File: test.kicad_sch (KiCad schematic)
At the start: 1 part

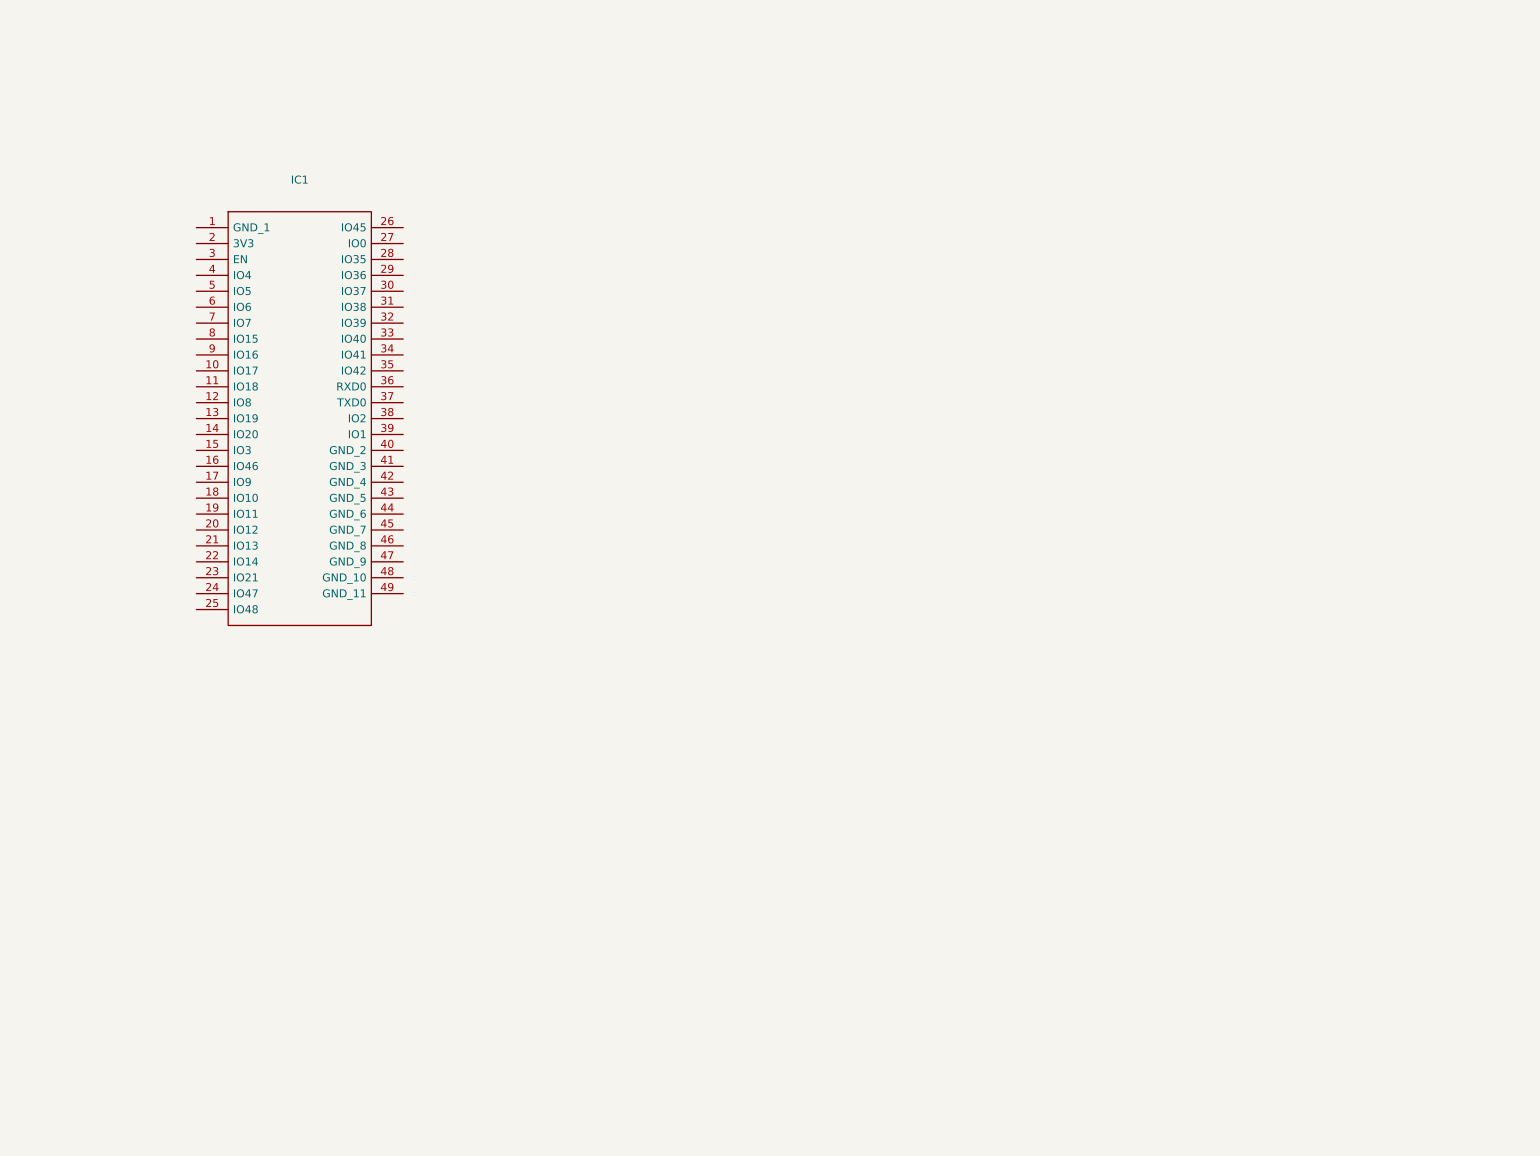
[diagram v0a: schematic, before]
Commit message: esp32 and power
added first try of battery, connecotrs and esp32.
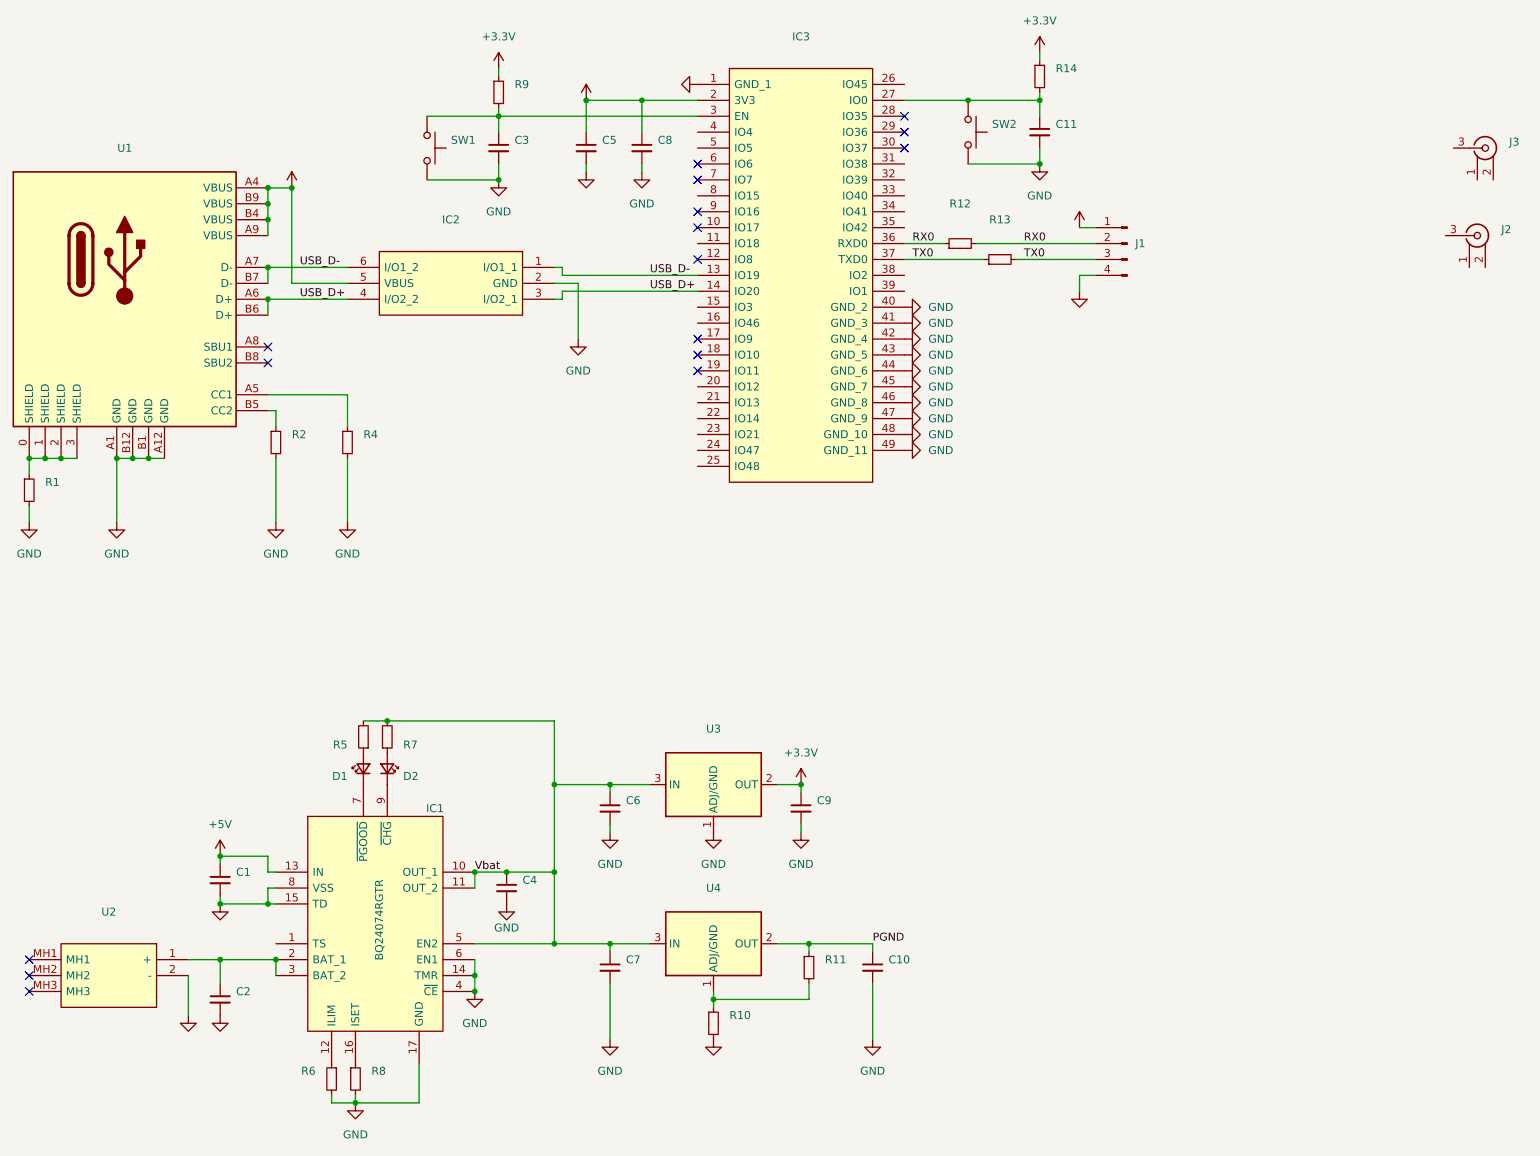
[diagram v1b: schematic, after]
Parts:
- added C1, C10, C11, C2, C3, C4, C5, C6, C7, C8, C9: (no value), symbol Device:C_Small
- added D1, D2: (no value), symbol Device:LED_Small
- added IC1: BQ24074RGTR, project_library:BQ24074RGTR, symbol project_library:BQ24074RGTR
- added IC2: (no value), symbol project_library:USBLC6-2SC6
- added J1: (no value), symbol Connector:Conn_01x04_Male
- added J2, J3: (no value), symbol project_library:73100-0105
- added R1, R10, R11, R12, R13, R14, R2, R4, R5, R6, R7, R8, R9: (no value), symbol Device:R_Small
- added SW1, SW2: (no value), symbol Switch:SW_Push
- added U1: (no value), symbol project_library:USB-TYPE-C-018
- added U2: (no value), symbol project_library:1043
- added U3, U4: (no value), symbol Regulator_Linear:LD1086DT33TR
- IC3: renamed from IC1; footprint project_library:ESP32-S3-WROOM-1 -> (none)
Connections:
- net GND: now reaches IC3.1 (GND_1)
- net GND: now also IC3.40 (GND_2), IC3.41 (GND_3), IC3.42 (GND_4), IC3.43 (GND_5), IC3.44 (GND_6), IC3.45 (GND_7), IC3.46 (GND_8), IC3.47 (GND_9), IC3.48 (GND_10), IC3.49 (GND_11), C1.2, C10.2, C11.2, C2.2, C3.2, C4.2, C5.2, C6.2, C7.2, C8.2, C9.2, IC1.14 (TMR), IC1.15 (TD), IC1.17 (GND), IC1.4 (~{CE}), IC1.6 (EN1), IC1.8 (VSS), IC2.2 (GND), J1.4 (Pin_4), R1.2, R10.2, R2.2, R4.2, R6.2, R8.2, SW1.2, SW2.2, U1.A1 (GND), U1.A12 (GND), U1.B1 (GND), U1.B12 (GND), U2.2 (-), U3.1 (ADJ/GND)
- net USB_D-: now reaches IC3.13 (IO19)
- net USB_D-: now also IC2.1 (I/O1_1), IC2.6 (I/O1_2), U1.A7 (D-), U1.B7 (D-)
- net USB_D+: now reaches IC3.14 (IO20)
- net USB_D+: now also IC2.3 (I/O2_1), IC2.4 (I/O2_2), U1.A6 (D+), U1.B6 (D+)
- net +3V3: now reaches IC3.2 (3V3)
- net +3V3: now also C5.1, C8.1, C9.1, J1.1 (Pin_1), R14.1, R9.1, U3.2 (OUT)
- net at IC3.27 (IO0): now also C11.1, R14.2, SW2.1
- net at IC3.3 (EN): now also C3.1, R9.2, SW1.1
- net RX0: now reaches IC3.36 (RXD0)
- net RX0: now also J1.2 (Pin_2), R12.1, R12.2
- net TX0: now reaches IC3.37 (TXD0)
- net TX0: now also J1.3 (Pin_3), R13.1, R13.2
- new net: R1.1, U1.0 (SHIELD), U1.1 (SHIELD), U1.2 (SHIELD), U1.3 (SHIELD)
- new net: D1.1 (K), IC1.7 (~{PGOOD})
- new net: D1.2 (A), R5.1
- new net: D2.1 (K), IC1.9 (~{CHG})
- new net: D2.2 (A), R7.1
- new net: R4.1, U1.A5 (CC1)
- new net: R2.1, U1.B5 (CC2)
- new net: IC1.12 (ILIM), R6.1
- new net: IC1.16 (ISET), R8.1
- new net: C2.1, IC1.2 (BAT_1), IC1.3 (BAT_2), U2.1 (+)
- new net: R10.1, R11.2, U4.1 (ADJ/GND)
- new net +5V: C1.1, IC1.13 (IN), IC2.5 (VBUS), U1.A4 (VBUS), U1.A9 (VBUS), U1.B4 (VBUS), U1.B9 (VBUS)
- new net PGND: C10.1, R11.1, U4.2 (OUT)
- new net Vbat: C4.1, C6.1, C7.1, IC1.10 (OUT_1), IC1.11 (OUT_2), IC1.5 (EN2), R5.2, R7.2, U3.3 (IN), U4.3 (IN)
- no-connect marks 0 -> 16

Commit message: first try of front end
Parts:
- added C?: 47n, Capacitor_SMD:C_1206_3216Metric_Pad1.33x1.80mm_HandSolder, symbol Device:C_Small
- added C? (x2): (no value), symbol Device:C_Small
- added C?: 100n, symbol Device:C_Small
- added C?: (no value), Capacitor_SMD:C_1206_3216Metric_Pad1.33x1.80mm_HandSolder, symbol Device:C_Small
- added C?: 5.5p-30p var, project_library:JZ300, symbol Device:C_Small
- added IC?: (no value), symbol project_library:MAX19506ETM+
- added IC?: (no value), symbol project_library:MCP6S91-E_MS
- added K1: (no value), symbol project_library:AQY210EHA
- added K?: AQY210EHA, project_library:AQY210EHAX, symbol project_library:AQY210EHA
- added R?: 100k, Resistor_SMD:R_1206_3216Metric_Pad1.30x1.75mm_HandSolder, symbol Device:R_Small
- added R?: (no value), symbol Device:R_Small
- added R?: (no value), Resistor_SMD:R_1206_3216Metric_Pad1.30x1.75mm_HandSolder, symbol Device:R_Small
- added R?: 910k, symbol Device:R_Small
- added U2: 1043, project_library:1043, symbol project_library:1043
- IC1: value BQ24074RGTR -> (none); footprint project_library:BQ24074RGTR -> (none)
- renumbered R11 to R10, R12 to R11, R13 to R12, R14 to R13, R6 to R3, R8 to R5, R5 to R6, R9 to R8, R10 to R9, U2 to U3, U3 to U4, U4 to U5
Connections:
- net GND: now also U2.2 (-)
- net PGND: now also J2.1, J2.2, J3.1, J3.2, C?.2, C?.2, R?.2, R?.2
- net USB_D+: no longer IC2.4 (I/O2_2), U1.A6 (D+), U1.B6 (D+)
- net USB_D-: no longer IC2.6 (I/O1_2), U1.A7 (D-), U1.B7 (D-)
- net at J2.3: now also C?.1, R?.1
- net at C2.1, IC1.2 (BAT_1), IC1.3 (BAT_2)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: now also U2.1 (+)
- net MISO: now reaches IC3.20 (IO12)
- net MOSI: now reaches IC3.21 (IO13)
- net SCLK: now reaches IC3.22 (IO14)
- net CS: now reaches IC3.8 (IO15)
- net at J3.3: now also C?.1, R?.1
- new net: C?.1, C?.2, K1.1 (Anode), R?.2
- new net: C?.1, C?.2, K1.2 (Kathode), R?.1
- new net: C?.1, C?.2, K?.2 (Kathode), R?.1
- new net: IC2.4 (I/O2_2), U1.A6 (D+), U1.B6 (D+)
- new net: IC2.6 (I/O1_2), U1.A7 (D-), U1.B7 (D-)
- new net: C?.1, C?.2, K?.1 (Anode), R?.2
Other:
- moved on the sheet: J2, J3, U3

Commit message: test changes
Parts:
- added C? (x2): 10u, Capacitor_SMD:C_1206_3216Metric_Pad1.33x1.80mm_HandSolder, symbol Device:C_Small
- added U?: LD1086DT33TR, Package_TO_SOT_SMD:TO-252-2, symbol Regulator_Linear:LD1086DT33TR
- C1: value (none) -> 1u; footprint (none) -> Capacitor_SMD:C_1206_3216Metric_Pad1.33x1.80mm_HandSolder
- C10, C6, C7, C9: value (none) -> 10u; footprint (none) -> Capacitor_SMD:C_1206_3216Metric_Pad1.33x1.80mm_HandSolder
- C11, C3: value (none) -> 100n; footprint (none) -> Capacitor_SMD:C_1206_3216Metric_Pad1.33x1.80mm_HandSolder
- C2, C4: value (none) -> 4u7; footprint (none) -> Capacitor_SMD:C_1206_3216Metric_Pad1.33x1.80mm_HandSolder
- C5: value (none) -> 22u; footprint (none) -> Capacitor_SMD:C_1206_3216Metric_Pad1.33x1.80mm_HandSolder
- C8: value (none) -> 0.1u; footprint (none) -> Capacitor_SMD:C_1206_3216Metric_Pad1.33x1.80mm_HandSolder
- C?: value (none) -> 100n
- C?: value (none) -> 5.5p-30p var; footprint (none) -> project_library:JZ300
- C?: value (none) -> 47n
- D1: value (none) -> LED_PowerOn?; footprint (none) -> LED_SMD:LED_2512_6332Metric_Pad1.52x3.35mm_HandSolder
- D2: value (none) -> LED_Charging; footprint (none) -> LED_SMD:LED_2512_6332Metric_Pad1.52x3.35mm_HandSolder
- IC1: value (none) -> BQ24074RGTR; footprint (none) -> project_library:BQ24074RGTR
- IC2: value (none) -> USBLC6-2SC6; footprint (none) -> project_library:USBLC6-2SC6
- IC3: value (none) -> ESP32-S3-WROOM-1-N16; footprint (none) -> project_library:ESP32-S3-WROOM-1
- IC?: value (none) -> MAX19506ETM+; footprint (none) -> QFN50P700X700X80-49N
- IC?: value (none) -> MCP6S91-E_MS; footprint (none) -> project_library:MCP6S91-E_MS
- J1: value (none) -> UART0; footprint (none) -> Connector_PinHeader_2.54mm:PinHeader_1x04_P2.54mm_Vertical
- J2, J3: value (none) -> 73100-0105; footprint (none) -> 73100-0105
- K1: value (none) -> AQY210EHA; footprint (none) -> project_library:AQY210EHAX
- R1: value (none) -> 1M; footprint (none) -> Resistor_SMD:R_1206_3216Metric_Pad1.30x1.75mm_HandSolder
- R10: value (none) -> 120; footprint (none) -> Resistor_SMD:R_1206_3216Metric_Pad1.30x1.75mm_HandSolder
- R11, R12: value (none) -> 470; footprint (none) -> Resistor_SMD:R_1206_3216Metric_Pad1.30x1.75mm_HandSolder
- R13, R2, R4, R8: value (none) -> 5k1; footprint (none) -> Resistor_SMD:R_1206_3216Metric_Pad1.30x1.75mm_HandSolder
- R3: value (none) -> 1k; footprint (none) -> Resistor_SMD:R_1206_3216Metric_Pad1.30x1.75mm_HandSolder
- R5: value (none) -> 820; footprint (none) -> Resistor_SMD:R_1206_3216Metric_Pad1.30x1.75mm_HandSolder
- R6, R7: value (none) -> 1k5; footprint (none) -> Resistor_SMD:R_1206_3216Metric_Pad1.30x1.75mm_HandSolder
- R9: value (none) -> 39; footprint (none) -> Resistor_SMD:R_1206_3216Metric_Pad1.30x1.75mm_HandSolder
- R?: value (none) -> 910k
- R?: value (none) -> 100k
- SW1: value (none) -> Reset; footprint (none) -> project_library:SW_TS-1187A-B-A-B
- SW2: value (none) -> Boot; footprint (none) -> project_library:SW_TS-1187A-B-A-B
- U1: value (none) -> USB-TYPE-C-018; footprint (none) -> project_library:USB-TYPE-C-018
- U3: value (none) -> 1043; footprint (none) -> project_library:1043
- U4, U5: value (none) -> LD1086DT33TR; footprint (none) -> Package_TO_SOT_SMD:TO-252-2
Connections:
- net +3V3: now also C?.1, U?.2 (OUT); no longer C9.1, U4.2 (OUT)
- net GND: now also C?.2, C?.2, U?.1 (ADJ/GND)
- net Vbat: now also C?.1, U?.3 (IN)
- new net +3.3VADC: C9.1, U4.2 (OUT)
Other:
- moved on the sheet: IC?

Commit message: added battery monitoring
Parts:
- removed R1: 1M, Resistor_SMD:R_1206_3216Metric_Pad1.30x1.75mm_HandSolder, symbol Device:R_Small
- added C?: 1u, Capacitor_SMD:C_1206_3216Metric_Pad1.33x1.80mm_HandSolder, symbol Device:C_Small
- added IC?: (no value), symbol project_library:LC709203FQH-01TWG
- added R?: (no value), Resistor_SMD:R_1206_3216Metric_Pad1.30x1.75mm_HandSolder, symbol Device:R_Small
- D1: value LED_PowerOn? -> (none)
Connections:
- net +5V: now also IC1.15 (TD)
- net GND: now also U1.0 (SHIELD), U1.1 (SHIELD), U1.2 (SHIELD), U1.3 (SHIELD), C?.1, IC?.1 (TEST), IC?.2 (VSS), IC?.9 (EP), R?.1; no longer IC1.15 (TD)
- net at C2.1, IC1.2 (BAT_1), IC1.3 (BAT_2)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: now also C?.2, IC?.3 (VDD)
- net ValidUSB: now reaches D1.1 (K), IC1.7 (~{PGOOD})
- net Charging: now reaches D2.1 (K), IC1.9 (~{CHG})
- net at IC1.1 (TS): now also R?.2
- new net Alarm: IC?.4 (ALARMB)
- new net SCL: IC?.8 (SCL)
- new net SDA: IC?.7 (SDA)
- no-connect marks 16 -> 21
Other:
- moved on the sheet: C1, C2, D1, D2, R6, R7, U2, U3

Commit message: change esp-pins for parallel adc input and correct bootstrap pins
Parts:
- removed C11: 100n, Capacitor_SMD:C_1206_3216Metric_Pad1.33x1.80mm_HandSolder, symbol Device:C_Small
- removed IC?: MAX19506ETM+, QFN50P700X700X80-49N, symbol project_library:MAX19506ETM+
- removed R13: 5k1, Resistor_SMD:R_1206_3216Metric_Pad1.30x1.75mm_HandSolder, symbol Device:R_Small
- C3: value 100n -> (none)
- D1: value (none) -> LED_ValidSource
- IC?: value (none) -> LC709203FQH-01TWG; footprint (none) -> project_library:LC709203FQH-01TWG
- R?: value (none) -> 10k
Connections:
- net Charging: now also IC3.35 (IO42)
- net MISO: no longer IC3.20 (IO12)
- net MOSI: now also IC3.19 (IO11); no longer IC3.21 (IO13)
- net SCL: now also IC3.38 (IO2)
- net SCLK: now also IC3.20 (IO12); no longer IC3.22 (IO14)
- net SDA: now also IC3.39 (IO1)
- net ENABLE: now reaches C3.1, IC3.3 (EN), R8.2, SW1.1
- net BOOT: now reaches IC3.27 (IO0), SW2.1
- net CH1_D6: now reaches IC3.10 (IO17)
- net CH1_D7: now reaches IC3.11 (IO18)
- net I2S_CLK: now reaches IC3.12 (IO8)
- net CH2_D0: now reaches IC3.15 (IO3)
- net LOG: now reaches IC3.16 (IO46)
- net CH2_D1: now reaches IC3.17 (IO9)
- net CH2_D2: now reaches IC3.18 (IO10)
- net CH2_D5: now reaches IC3.23 (IO21)
- net CH2_D6: now reaches IC3.24 (IO47)
- net CH2_D7: now reaches IC3.25 (IO48)
- net VSPI: now reaches IC3.26 (IO45)
- net CH1_Gnd_Sel: now reaches IC3.31 (IO38)
- net CH2_Gnd_Sel: now reaches IC3.32 (IO39)
- net CS_A: now reaches IC3.33 (IO40)
- net CS_B: now reaches IC3.34 (IO41)
- net CH1_D0: now reaches IC3.4 (IO4)
- net CH1_D1: now reaches IC3.5 (IO5)
- net CH1_D2: now reaches IC3.6 (IO6)
- net CH1_D3: now reaches IC3.7 (IO7)
- net CH1_D5: now reaches IC3.9 (IO16)
- net CS renamed CH1_D4
- new net CH2_D3: IC3.21 (IO13)
- new net CH2_D4: IC3.22 (IO14)
- no-connect marks 21 -> 15
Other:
- note added: "PSRAM (S.11)"
- moved on the sheet: C3, C5, C8, J1, R11, R12, R8, SW1, SW2
